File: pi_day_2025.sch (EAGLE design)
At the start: 102 parts, among them IC1 W25Q64JVXGIQ, J4 SM03B-SRSS-TB(LF)(SN), Q2 310mA/60V/1.6Ω, U1 APS6404L-3SQR-ZR, U2 RP2350A, U3 TPS76318DBVRG4, U4 TPS63001DRCR, U5 TXS0108EPWRG4, U6 LSM6DS3TR-C, U7 MCP73833T-AMI/MF, U8 TPS2113APWR, Y1 12MHz

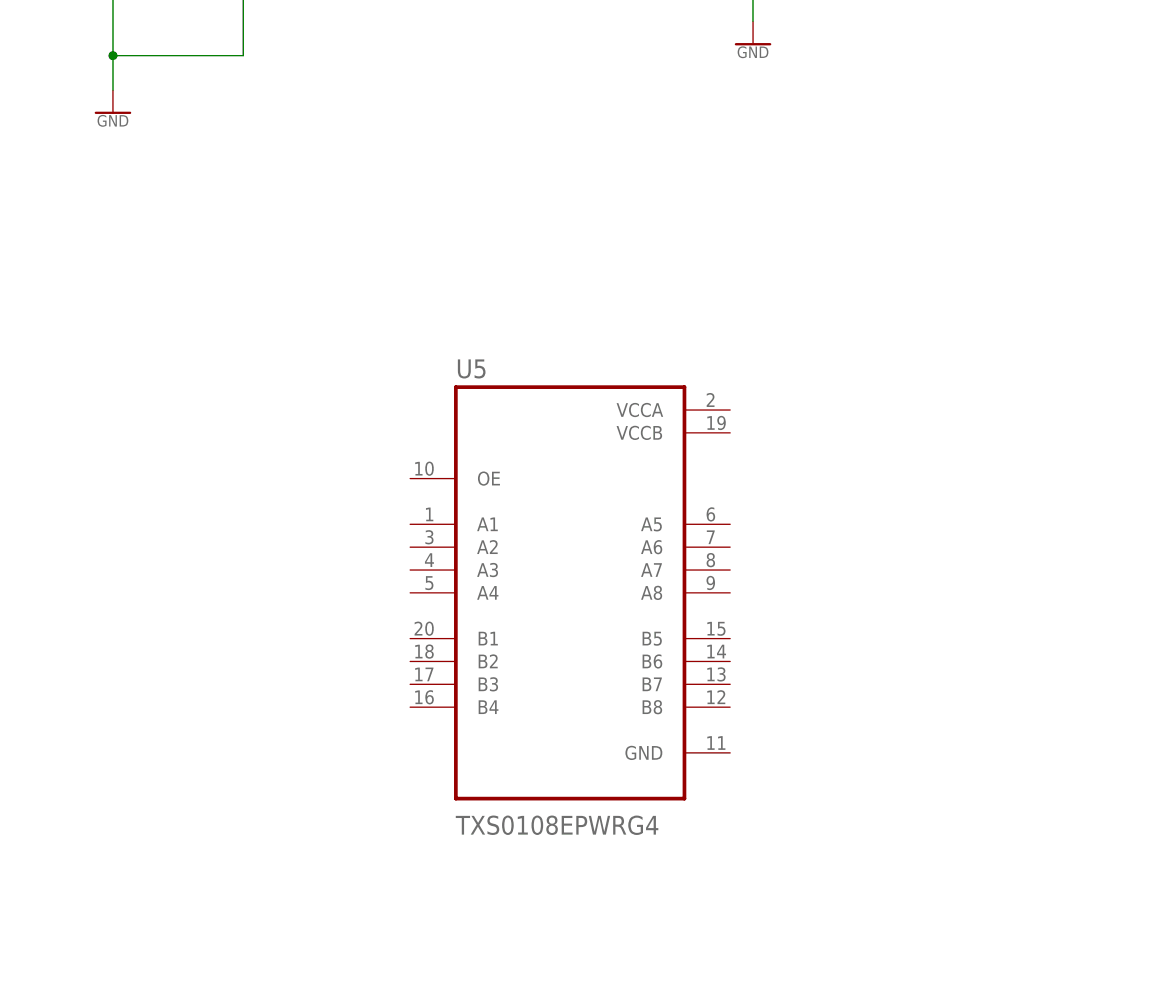
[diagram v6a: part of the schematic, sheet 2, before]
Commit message: additions to txs0108
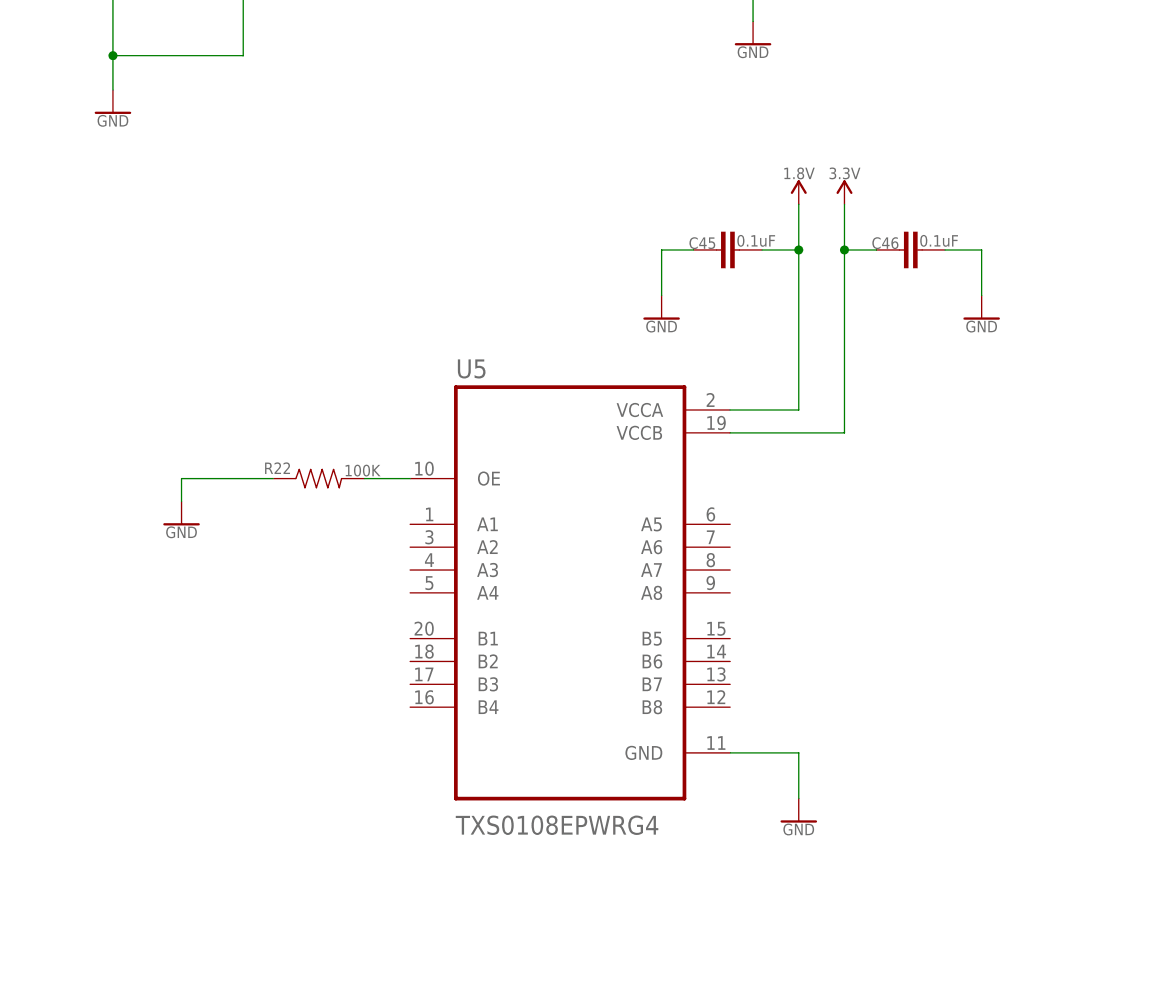
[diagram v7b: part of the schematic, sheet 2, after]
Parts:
- added C45, C46: 0.1uF, SparkFun-Capacitors:0.1UF-0402-6.3V-10%-X7R
- added R22: 100K, SparkFun-Resistors:100KOHM-0402-1/16W-1%
- R14: value 500 -> (none)
- R3, R8: value 5.1K -> (none)
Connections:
- new net N$24: R22.2, U5.OE
- net 1.8V: now also C45.2, U5.VCCA
- net 3.3V: now also C46.1, U5.VCCB
- net GND: now also C45.1, C46.2, R22.1, U5.GND

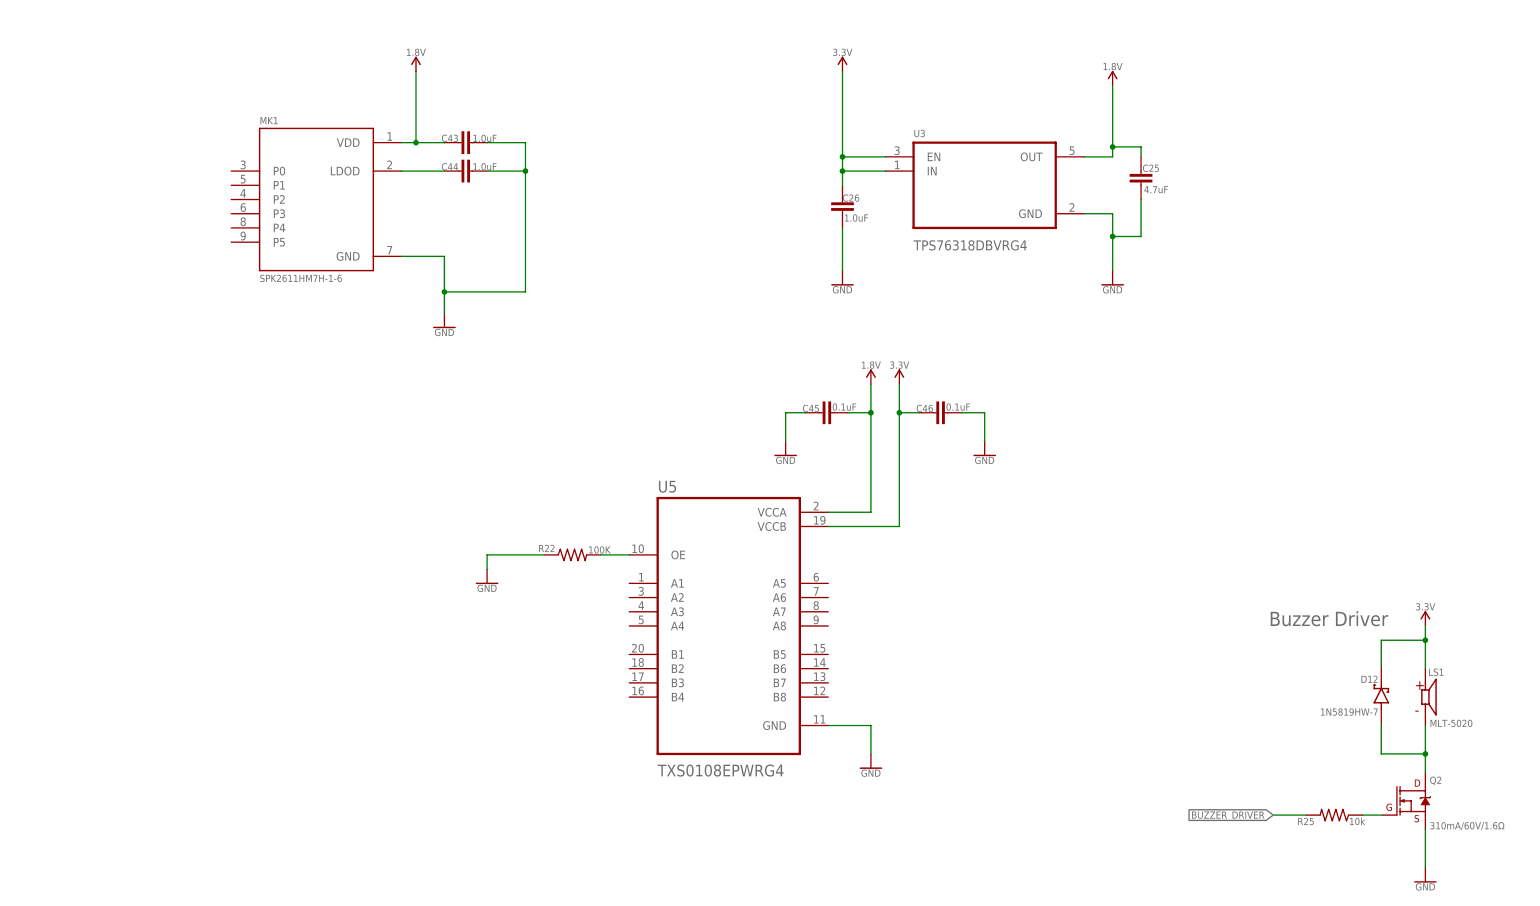
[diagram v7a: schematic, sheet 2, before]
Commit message: Added pinouts for IA611 & voltage level converter
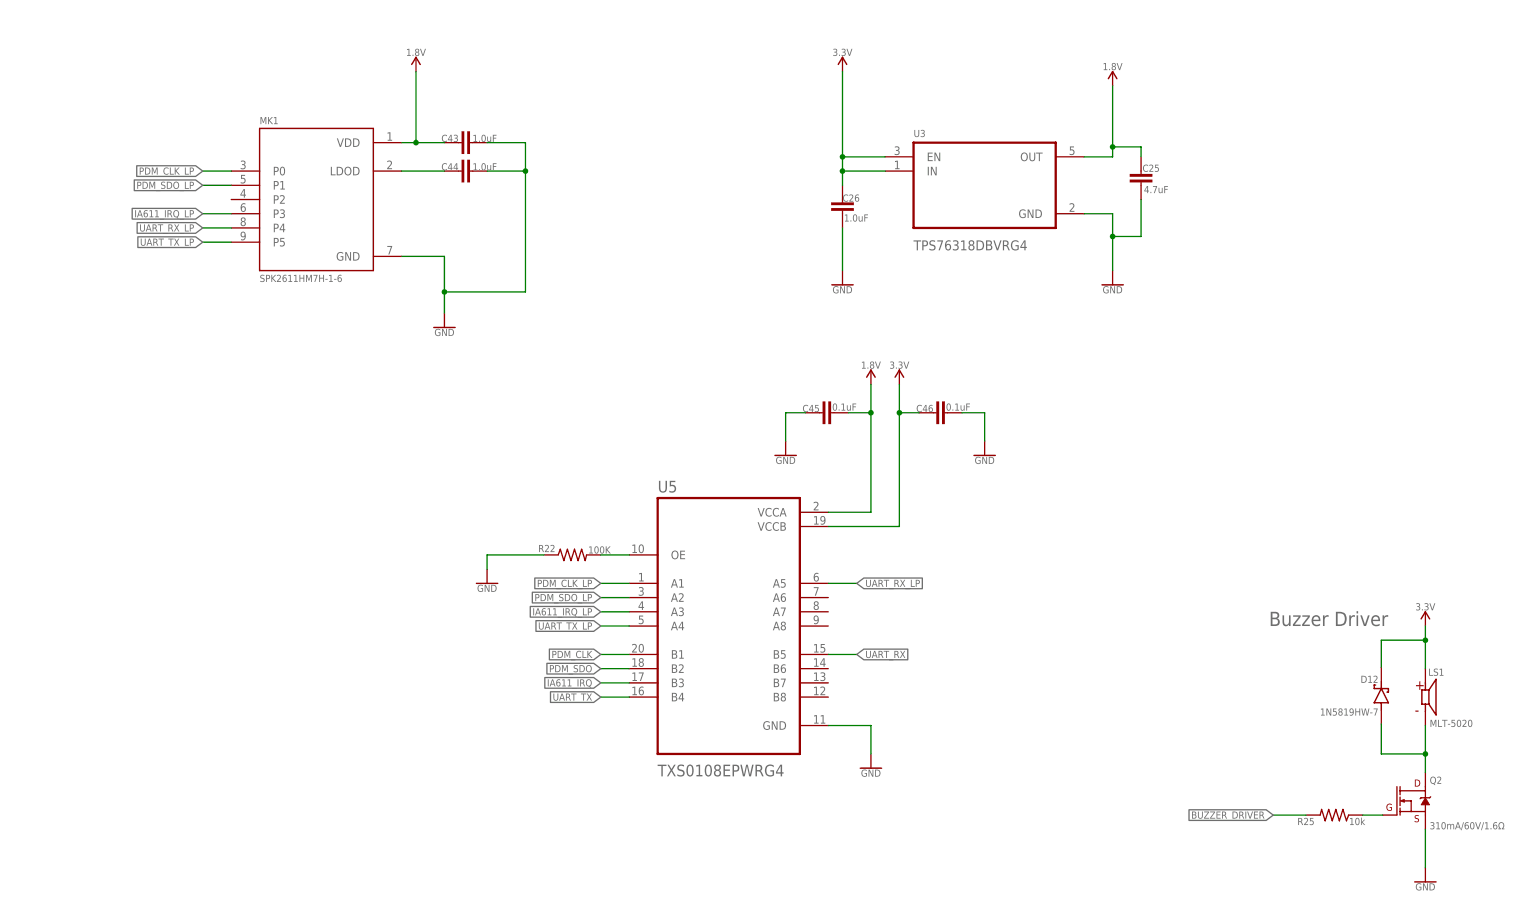
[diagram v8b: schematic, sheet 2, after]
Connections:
- new net IA611_IRQ: U5.B3
- new net IA611_IRQ_LP: MK1.P3, U5.A3
- new net PDM_CLK: U5.B1
- new net PDM_CLK_LP: MK1.P0, U5.A1
- new net PDM_SDO: U5.B2
- new net PDM_SDO_LP: MK1.P1, U5.A2
- new net UART_RX: U5.B5
- new net UART_RX_LP: MK1.P4, U5.A5
- new net UART_TX: U5.B4
- new net UART_TX_LP: MK1.P5, U5.A4
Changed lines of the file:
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@@
+</segment>
+</net>
+<net name="PDM_CLK_LP" class="0">
+<segment>
+<pinref part="MK1" gate="G$1" pin="P0"/>
+<wire x1="43.18" y1="149.86" x2="38.1" y2="149.86" width="0.1524" layer="91"/>
+<label x="38.1" y="149.86" size="1.27" layer="95" font="vector" ratio="20" rot="R180" xref="yes"/>
+</segment>
+<segment>
+<pinref part="U5" gate="G$1" pin="A1"/>
+<wire x1="114.3" y1="76.2" x2="109.22" y2="76.2" width="0.1524" layer="91"/>
+<label x="109.22" y="76.2" size="1.27" layer="95" font="vector" ratio="20" rot="R180" xref="yes"/>
+</segment>
+</net>
+<net name="PDM_SDO_LP" class="0">
+<segment>
+<pinref part="MK1" gate="G$1" pin="P1"/>
+<wire x1="43.18" y1="147.32" x2="38.1" y2="147.32" width="0.1524" layer="91"/>
+<label x="38.1" y="147.32" size="1.27" layer="95" font="vector" ratio="20" rot="R180" xref="yes"/>
+</segment>
+<segment>
+<pinref part="U5" gate="G$1" pin="A2"/>
+<wire x1="114.3" y1="73.66" x2="109.22" y2="73.66" width="0.1524" layer="91"/>
+<label x="109.22" y="73.66" size="1.27" layer="95" font="vector" ratio="20" rot="R180" xref="yes"/>
+</segment>
+</net>
+<net name="IA611_IRQ_LP" class="0">
+<segment>
+<pinref part="MK1" gate="G$1" pin="P3"/>
+<wire x1="43.18" y1="142.24" x2="38.1" y2="142.24" width="0.1524" layer="91"/>
+<label x="38.1" y="142.24" size="1.27" layer="95" font="vector" ratio="20" rot="R180" xref="yes"/>
+</segment>
+<segment>
+<pinref part="U5" gate="G$1" pin="A3"/>
+<wire x1="114.3" y1="71.12" x2="109.22" y2="71.12" width="0.1524" layer="91"/>
+<label x="109.22" y="71.12" size="1.27" layer="95" font="vector" ratio="20" rot="R180" xref="yes"/>
+</segment>
+</net>
+<net name="UART_RX_LP" class="0">
+<segment>
+<pinref part="MK1" gate="G$1" pin="P4"/>
+<wire x1="43.18" y1="139.7" x2="38.1" y2="139.7" width="0.1524" layer="91"/>
+<label x="38.1" y="139.7" size="1.27" layer="95" font="vector" ratio="20" rot="R180" xref="yes"/>
+</segment>
+<segment>
+<pinref part="U5" gate="G$1" pin="A5"/>
+<wire x1="149.86" y1="76.2" x2="154.94" y2="76.2" width="0.1524" layer="91"/>
+<label x="154.94" y="76.2" size="1.27" layer="95" font="vector" ratio="20" xref="yes"/>
+</segment>
+</net>
+<net name="UART_TX_LP" class="0">
+<segment>
+<pinref part="MK1" gate="G$1" pin="P5"/>
+<wire x1="43.18" y1="137.16" x2="38.1" y2="137.16" width="0.1524" layer="91"/>
+<label x="38.1" y="137.16" size="1.27" layer="95" font="vector" ratio="20" rot="R180" xref="yes"/>
+</segment>
+<segment>
+<pinref part="U5" gate="G$1" pin="A4"/>
+<wire x1="114.3" y1="68.58" x2="109.22" y2="68.58" width="0.1524" layer="91"/>
+<label x="109.22" y="68.58" size="1.27" layer="95" font="vector" ratio="20" rot="R180" xref="yes"/>
+</segment>
+</net>
+<net name="PDM_CLK" class="0">
+<segment>
+<pinref part="U5" gate="G$1" pin="B1"/>
+<wire x1="114.3" y1="63.5" x2="109.22" y2="63.5" width="0.1524" layer="91"/>
+<label x="109.22" y="63.5" size="1.27" layer="95" font="vector" ratio="20" rot="R180" xref="yes"/>
+</segment>
+</net>
+<net name="PDM_SDO" class="0">
+<segment>
+<pinref part="U5" gate="G$1" pin="B2"/>
+<wire x1="114.3" y1="60.96" x2="109.22" y2="60.96" width="0.1524" layer="91"/>
+<label x="109.22" y="60.96" size="1.27" layer="95" font="vector" ratio="20" rot="R180" xref="yes"/>
+</segment>
+</net>
+<net name="IA611_IRQ" class="0">
+<segment>
+<pinref part="U5" gate="G$1" pin="B3"/>
+<wire x1="114.3" y1="58.42" x2="109.22" y2="58.42" width="0.1524" layer="91"/>
+<label x="109.22" y="58.42" size="1.27" layer="95" font="vector" ratio="20" rot="R180" xref="yes"/>
+</segment>
+</net>
+<net name="UART_TX" class="0">
+<segment>
+<pinref part="U5" gate="G$1" pin="B4"/>
+<wire x1="114.3" y1="55.88" x2="109.22" y2="55.88" width="0.1524" layer="91"/>
+<label x="109.22" y="55.88" size="1.27" layer="95" font="vector" ratio="20" rot="R180" xref="yes"/>
+</segment>
+</net>
+<net name="UART_RX" class="0">
+<segment>
+<pinref part="U5" gate="G$1" pin="B5"/>
+<wire x1="149.86" y1="63.5" x2="154.94" y2="63.5" width="0.1524" layer="91"/>
+<label x="154.94" y="63.5" size="1.27" layer="95" font="vector" ratio="20" xref="yes"/>
 </segment>
 </net>
